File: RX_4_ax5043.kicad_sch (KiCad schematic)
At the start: 19 parts, among them P4 CONUFL001-SMD-T, Q6 DMP2037U-7, U19 AX5043

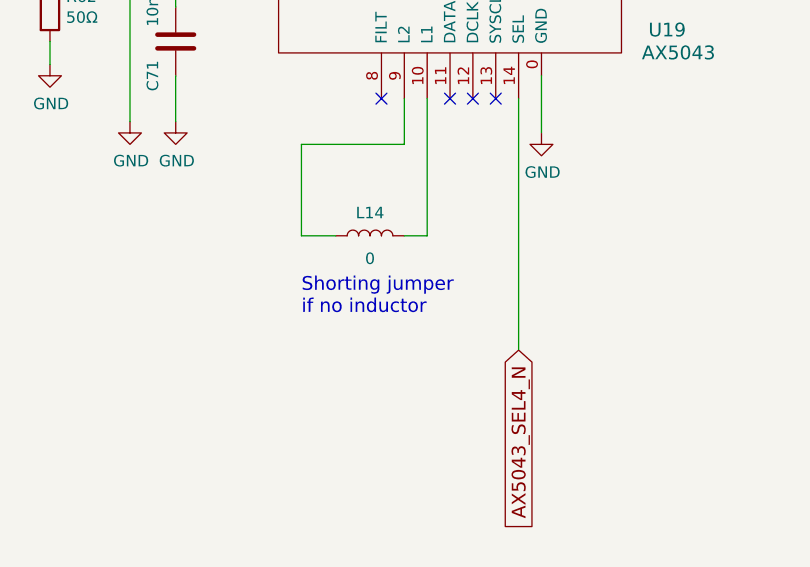
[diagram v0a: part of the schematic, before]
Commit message: Update schematics to match what is done to the boards so far
Get ready to split off a branch where the updates to the board can be
done while still keeping updates for the prototypes.

Signed-off-by: Corey Minyard <corey@minyard.net>
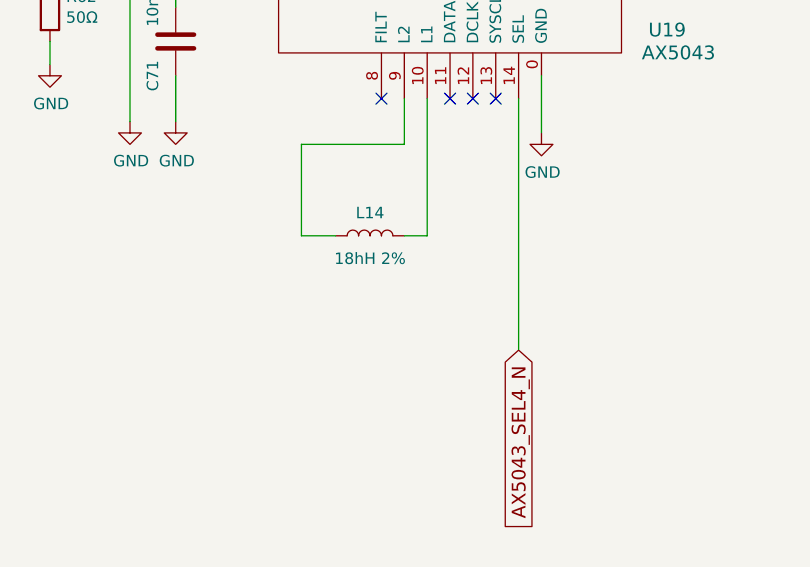
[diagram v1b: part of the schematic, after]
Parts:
- L14: value 0 -> 18hH 2%
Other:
- note removed: "Shorting jumper if no inductor"
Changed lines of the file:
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@@
-		)
-	)
-	(text "Shorting jumper\nif no inductor"
-		(exclude_from_sim no)
-		(at 200.66 180.34 0)
-		(effects
-			(font
-				(size 1.524 1.524)
-			)
-			(justify left bottom)
 		)
 	)
@@
 			)
 		)
-		(property "Value" "0"
+		(property "Value" "18hH 2%"
 			(at 208.28 173.99 90)
 			(effects

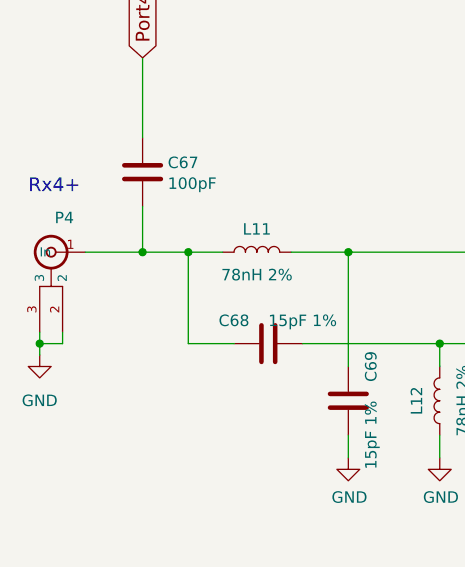
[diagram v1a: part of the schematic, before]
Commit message: Clean up the U.FL connectors a little more
Re-add the ones for TX/RX so both MMCX and U.FL are available.

Move P8 to a better location.

Signed-off-by: Corey Minyard <corey@minyard.net>
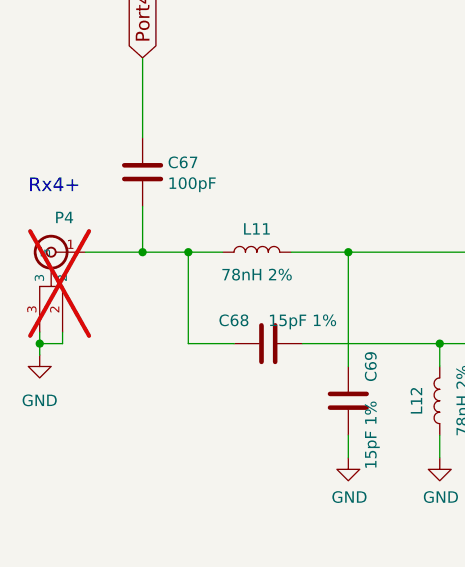
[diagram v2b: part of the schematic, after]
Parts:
- P4: now not fitted; now left out of the parts list
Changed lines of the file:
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@@
 		(unit 1)
 		(exclude_from_sim no)
-		(in_bom yes)
+		(in_bom no)
 		(on_board yes)
-		(dnp no)
+		(dnp yes)
 		(property "Reference" "P4"
 			(at 111.76 121.92 0)

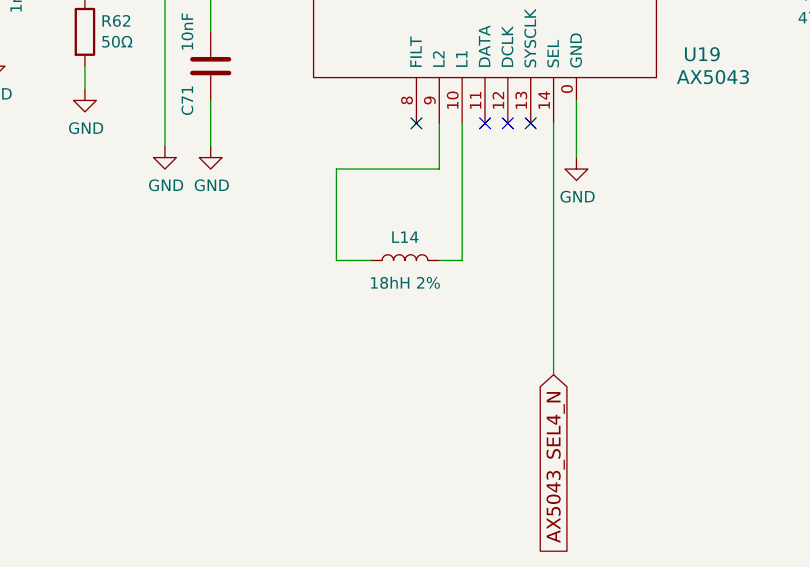
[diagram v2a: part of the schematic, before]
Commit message: Clean up BOM issues
Fix missing parts and mistypes parts.

Signed-off-by: Corey Minyard <corey@minyard.net>
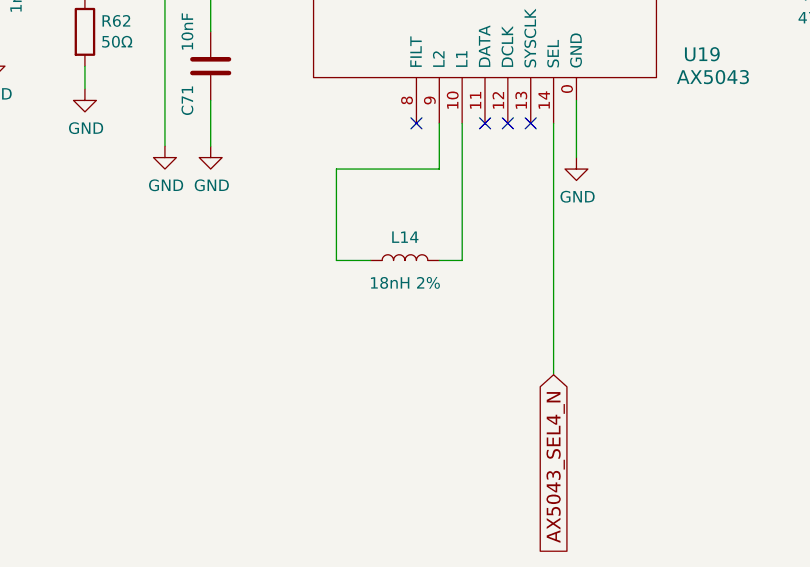
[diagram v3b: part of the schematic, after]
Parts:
- L14: value 18hH 2% -> 18nH 2%
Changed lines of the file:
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@@
 			)
 		)
-		(property "Value" "18hH 2%"
+		(property "Value" "18nH 2%"
 			(at 208.28 173.99 90)
 			(effects

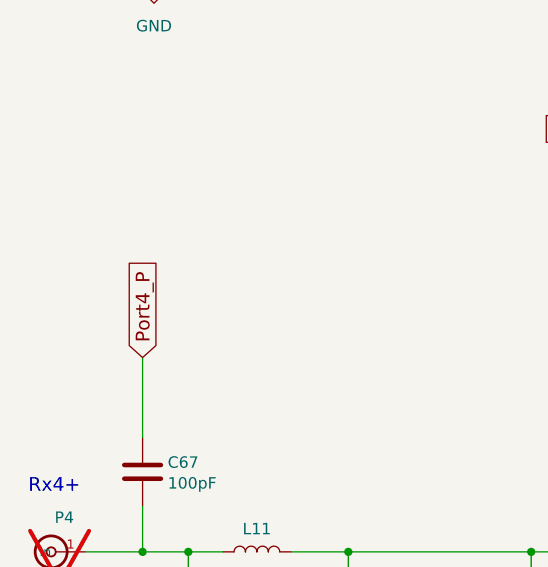
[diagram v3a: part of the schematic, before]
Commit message: Run the extra GPIOs to the PC104
They were recently freed with the ABF rework, use them.

Also, a kicad update broke some stuff, fix it.

Signed-off-by: Corey Minyard <corey@minyard.net>
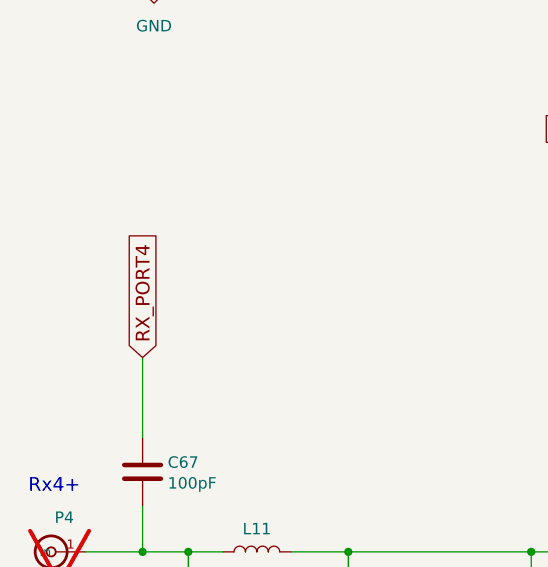
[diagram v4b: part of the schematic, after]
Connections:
- net Port4_P renamed RX_PORT4
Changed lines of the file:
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@@
 		)
 	)
-	(global_label "Port4_P"
+	(global_label "RX_PORT4"
 		(shape input)
 		(at 119.38 104.14 90)
@@
 		)
 		(property "Intersheetrefs" "${INTERSHEET_REFS}"
-			(at 119.38 92.4895 90)
+			(at 119.38 89.9496 90)
 			(effects
 				(font

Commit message: Get the board ready for operation
Make the board ready as a final product, remove the lab testing portions
and add in the things required for full operation.

Signed-off-by: Corey Minyard <corey@minyard.net>
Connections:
- net AX5043_CLK renamed AX5043_SPI_CLK
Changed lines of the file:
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@@
 		)
 	)
-	(global_label "AX5043_CLK"
+	(global_label "AX5043_SPI_CLK"
 		(shape input)
 		(at 265.43 139.7 0)

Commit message: Parts replacements for out of stock parts
Signed-off-by: Corey Minyard <corey@minyard.net>
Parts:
- Q6: value DMP2037U-7 -> DMP2160UWQ-7; footprint Package_TO_SOT_SMD:SOT-23 -> Package_TO_SOT_SMD:SOT-323_SC-70
